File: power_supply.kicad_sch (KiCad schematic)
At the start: 0 parts

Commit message: power supply first draft
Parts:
- added C1: 1µ, symbol Device:C
- added D1: SML-P11UTT86R, LED_SMD:LED_0402_1005Metric, symbol Device:LED
- added J1: TYPE-C 16PIN L8.35, easyeda2kicad:TYPE-C-SMD_20009-UCAF001-X, symbol 0 __:TYPE-C16PINL8.35
- added Q1: AONS21321, 0__:DFN-8_L6.0-W5.0-P1.27-LS6.2-BL, symbol 0 __:AONS21321
- added R1: 10, symbol Device:R
- added R2: 5.1k, symbol Device:R
- added R3: 49.9k, symbol Device:R
- added R4: 4.53k, symbol Device:R
- added R5: 18k, symbol Device:R
- added U1: HUSB238_002DD, easyeda2kicad:DFN-10_L3.0-W3.0-P0.50-BL-EP2.5, symbol 0 __:HUSB238_002DD
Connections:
- new net: D1.2 (A), R5.2
- new net: Q1.4 (G), R2.1, R3.2
- new net: J1.A4 (VBUS), Q1.5 (D), R1.1, R3.1
- new net: J1.A5 (CC1), U1.4 (CC1)
- new net: J1.A6 (D+), J1.B6 (D+), U1.2 (D+)
- new net: J1.A7 (D-), J1.B7 (D-), U1.3 (D-)
- new net: J1.B5 (CC2), U1.5 (CC2)
- new net: C1.2, R1.2, U1.1 (VIN)
- new net: R4.1, U1.9 (ISET)
- new net: R2.2, U1.10 (GATE)
- new net GND: C1.1, D1.1 (K), J1.4 (Shield), J1.A1 (GND), R4.2, U1.11 (GND)
- new net VCC: Q1.1 (S), R5.1
- no-connect marks 0 -> 5

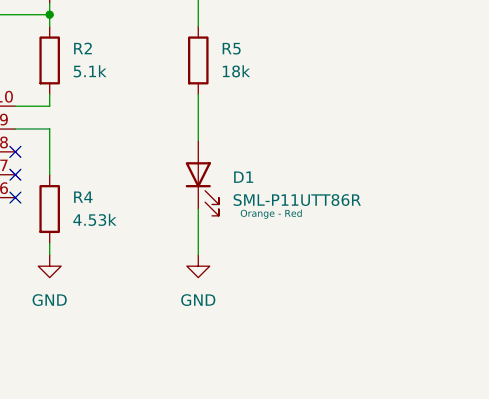
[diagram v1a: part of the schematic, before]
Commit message: Add output selector
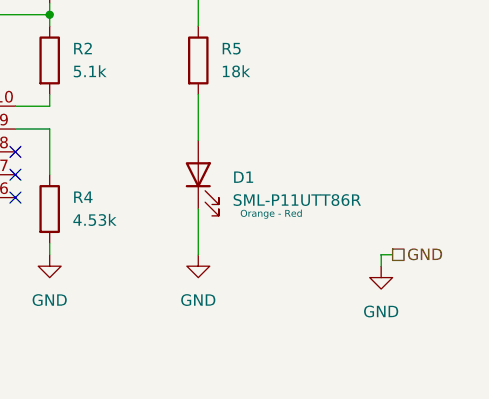
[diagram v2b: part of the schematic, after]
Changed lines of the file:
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@@
+	(wire
+		(pts
+			(xy 256.54 177.8) (xy 256.54 179.07)
+		)
+		(stroke
+			(width 0)
+			(type default)
+		)
+	)
 	(wire
 		(pts
@@
 		(pts
 			(xy 152.4 184.15) (xy 153.67 184.15)
+		)
+		(stroke
+			(width 0)
+			(type default)
+		)
+	)
+	(wire
+		(pts
+			(xy 257.81 177.8) (xy 256.54 177.8)
 		)
 		(stroke
@@
 		(shape passive)
 		(at 257.81 143.51 0)
+		(fields_autoplaced yes)
+		(effects
+			(font
+				(size 1.27 1.27)
+			)
+			(justify left)
+		)
+	)
+	(hierarchical_label "GND"
+		(shape passive)
+		(at 257.81 177.8 0)
 		(fields_autoplaced yes)
 		(effects
@@
 					(unit 1)
 				)
+			)
+		)
+	)
+	(symbol
+		(lib_id "power:GND")
+		(at 256.54 179.07 0)
+		(unit 1)
+		(exclude_from_sim no)
+		(in_bom yes)
+		(on_board yes)
+		(dnp no)
+		(fields_autoplaced yes)
+		(property "Reference" "#PWR019"
+			(at 256.54 185.42 0)
+			(effects
+				(font
+					(size 1.27 1.27)
+				)
+				(hide yes)
+			)
+		)
+		(property "Value" "GND"
+			(at 256.54 184.15 0)
+			(effects
+				(font
+					(size 1.27 1.27)
+				)
+			)
+		)
+		(property "Footprint" ""
+			(at 256.54 179.07 0)
+			(effects
+				(font
+					(size 1.27 1.27)
+				)
+				(hide yes)
+			)
+		)
+		(property "Datasheet" ""
+			(at 256.54 179.07 0)
+			(effects
+				(font
+					(size 1.27 1.27)
+				)
+				(hide yes)
+			)
+		)
+		(property "Description" "Power symbol creates a global label with name \"GND\" , ground"
+			(at 256.54 179.07 0)
+			(effects
+				(font
+					(size 1.27 1.27)
+				)
+				(hide yes)
+			)
+		)
+		(pin "1"
+		)
+		(instances
+			(project "AudioInterface"
+				(path "/0650c7a8-acba-429c-9f8e-eec0baf0bc1c/fede4c36-00cc-4d3d-b71c-5243ba232202/ae4f2c87-1f41-448f-be09-0b58202da066"
+					(reference "#PWR019")
+					(unit 1)
+				)

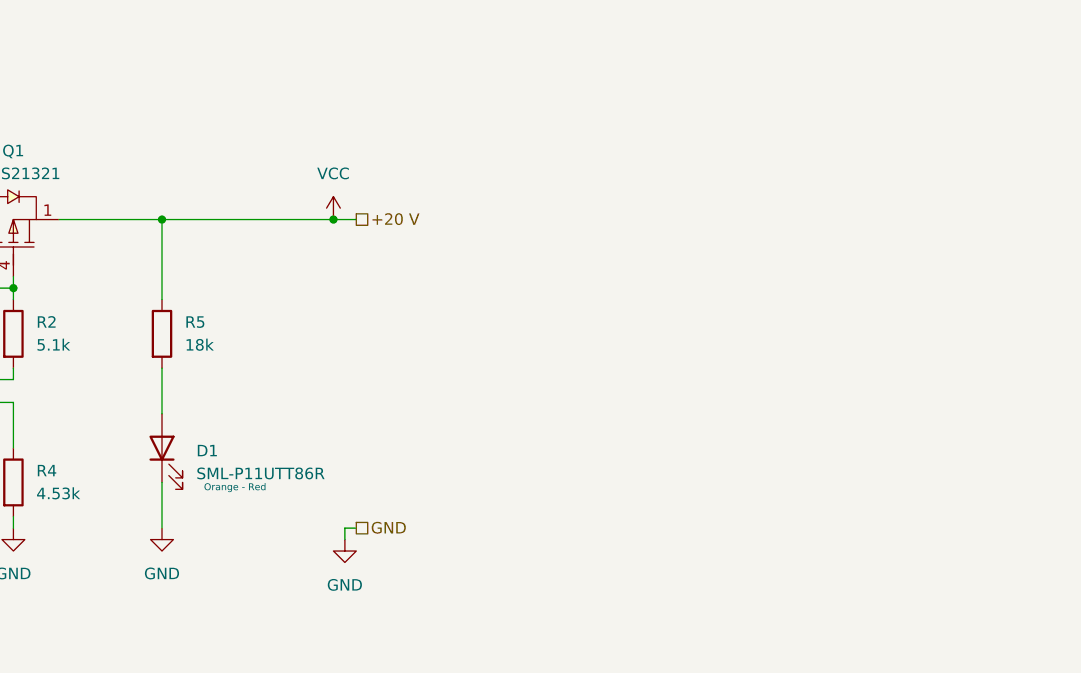
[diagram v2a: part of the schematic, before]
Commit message: add 5V regulator
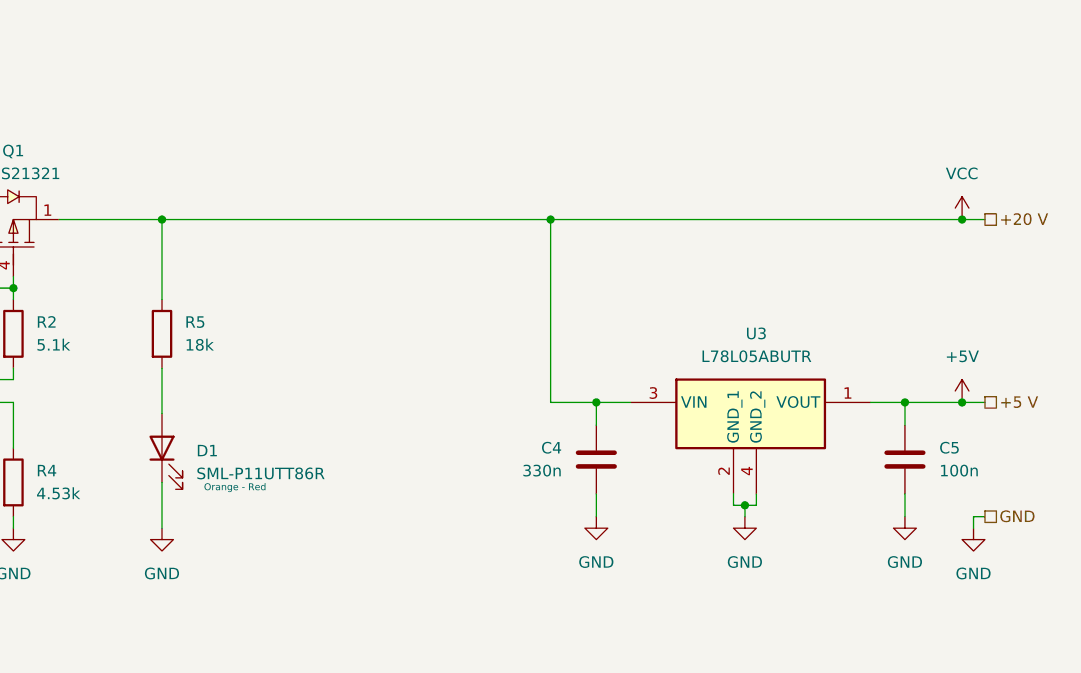
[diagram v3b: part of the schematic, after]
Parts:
- added C4: 330n, symbol Device:C
- added C5: 100n, symbol Device:C
- added U3: L78L05ABUTR, 0__:L78L05ABUTR, symbol 0 __:L78L05ABUTR
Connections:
- net GND: now also C4.1, C5.1, U3.2 (GND_1), U3.4 (GND_2)
- net VCC: now also C4.2, U3.3 (VIN)
- new net +5V: C5.2, U3.1 (VOUT)

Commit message: source component and fix some lib
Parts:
- C1: footprint (none) -> Capacitor_SMD:C_0402_1005Metric; LCSC Part (none) -> C1518208
- C4: footprint (none) -> Capacitor_SMD:C_0402_1005Metric; LCSC Part (none) -> C16193239
- C5: footprint (none) -> Capacitor_SMD:C_0402_1005Metric; LCSC Part (none) -> C77020
- D1: LCSC Part (none) -> C510300
- J1: footprint easyeda2kicad:TYPE-C-SMD_20009-UCAF001-X -> 0__:TYPE-C-SMD_20009-UCAF001-X
- R1: footprint (none) -> Resistor_SMD:R_0402_1005Metric; LCSC Part (none) -> C854481
- R2: footprint (none) -> Resistor_SMD:R_0603_1608Metric; LCSC Part (none) -> C413696
- R3: footprint (none) -> Resistor_SMD:R_0402_1005Metric; LCSC Part (none) -> C409918
- R4: footprint (none) -> Resistor_SMD:R_0402_1005Metric; LCSC Part (none) -> C416543
- R5: footprint (none) -> Resistor_SMD:R_0402_1005Metric; LCSC Part (none) -> C413008
- U1: footprint easyeda2kicad:DFN-10_L3.0-W3.0-P0.50-BL-EP2.5 -> 0__:DFN-10_L3.0-W3.0-P0.50-BL-EP2.5
- U3: LCSC Part (none) -> C42738
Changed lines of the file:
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@@
+			)
+		)
+		(property "LCSC Part" "C510300"
+			(at 236.22 168.91 0)
+			(effects
+				(font
+					(size 1.27 1.27)
+				)
+				(hide yes)
 			)
 		)
@@
 			)
 		)
-		(property "Footprint" "easyeda2kicad:TYPE-C-SMD_20009-UCAF001-X"
+		(property "Footprint" "0__:TYPE-C-SMD_20009-UCAF001-X"
 			(at 149.86 189.23 0)
 			(effects
@@
 			)
 		)
-		(property "Footprint" ""
+		(property "Footprint" "Capacitor_SMD:C_0402_1005Metric"
 			(at 188.2648 172.72 0)
 			(effects
@@
 			)
 		)
+		(property "LCSC Part" "C1518208"
+			(at 189.23 176.53 0)
+			(effects
+				(font
+					(size 1.27 1.27)
+				)
+				(hide yes)
+			)
+		)
 		(pin "2"
 		)
@@
 			)
 		)
-		(property "Footprint" ""
+		(property "Footprint" "Resistor_SMD:R_0402_1005Metric"
 			(at 217.932 172.72 90)
 			(effects
@@
 			)
 		)
+		(property "LCSC Part" " C416543"
+			(at 219.71 172.72 0)
+			(effects
+				(font
+					(size 1.27 1.27)
+				)
+				(hide yes)
+			)
+		)
 		(pin "1"
 		)
@@
 			)
 		)
-		(property "Footprint" ""
+		(property "Footprint" "Resistor_SMD:R_0603_1608Metric"
 			(at 217.932 156.21 90)
 			(effects
@@
 		)
 		(property "Description" "Resistor"
+			(at 219.71 156.21 0)
+			(effects
+				(font
+					(size 1.27 1.27)
+				)
+				(hide yes)
+			)
+		)
+		(property "LCSC Part" "C413696"
 			(at 219.71 156.21 0)
 			(effects
@@
 			)
 		)
-		(property "Footprint" ""
+		(property "Footprint" "Capacitor_SMD:C_0402_1005Metric"
 			(at 285.4452 166.37 0)
 			(effects
@@
 		)
 		(property "Description" "Unpolarized capacitor"
+			(at 284.48 170.18 0)
+			(effects
+				(font
+					(size 1.27 1.27)
+				)
+				(hide yes)
+			)
+		)
+		(property "LCSC Part" "C16193239"
 			(at 284.48 170.18 0)
 			(effects
@@
 			)
 		)
-		(property "Footprint" ""
+		(property "Footprint" "Resistor_SMD:R_0402_1005Metric"
 			(at 213.868 147.32 90)
 			(effects
@@
 			)
 		)
+		(property "LCSC Part" "C409918"
+			(at 212.09 147.32 0)
+			(effects
+				(font
+					(size 1.27 1.27)
+				)
+				(hide yes)
+			)
+		)
 		(pin "1"
 		)
@@
 			)
 		)
-		(property "Footprint" ""
+		(property "Footprint" "Resistor_SMD:R_0402_1005Metric"
 			(at 234.442 156.21 90)
 			(effects
@@
 			)
 		)
+		(property "LCSC Part" "C413008"
+			(at 236.22 156.21 0)
+			(effects
+				(font
+					(size 1.27 1.27)
+				)
+				(hide yes)
+			)
+		)
 		(pin "1"
 		)
@@
 			)
 		)
-		(property "Footprint" ""
+		(property "Footprint" "Resistor_SMD:R_0402_1005Metric"
 			(at 187.452 156.21 90)
 			(effects
@@
 			)
 		)
+		(property "LCSC Part" "C854481"
+			(at 189.23 156.21 0)
+			(effects
+				(font
+					(size 1.27 1.27)
+				)
+				(hide yes)
+			)
+		)
 		(pin "1"
 		)
@@
 				)
 				(justify left top)
+				(hide yes)
+			)
+		)
+		(property "LCSC Part" " C42738"
+			(at 288.29 163.83 0)
+			(effects
+				(font
+					(size 1.27 1.27)
+				)
 				(hide yes)
 			)
@@
 			)
 		)
-		(property "Footprint" "easyeda2kicad:DFN-10_L3.0-W3.0-P0.50-BL-EP2.5"
+		(property "Footprint" "0__:DFN-10_L3.0-W3.0-P0.50-BL-EP2.5"
 			(at 205.74 184.15 0)
 			(effects
@@
 			)
 		)
-		(property "Footprint" ""
+		(property "Footprint" "Capacitor_SMD:C_0402_1005Metric"
 			(at 317.8048 166.37 0)
 			(effects
@@
 			(at 318.77 170.18 0)
 			(effects
+				(font
+					(size 1.27 1.27)
+				)
+				(hide yes)
+			)
+		)
+		(property "LCSC Part" "C77020"
+			(at 318.77 170.18 0)
+			(effects
